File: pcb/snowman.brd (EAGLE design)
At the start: 69.4 x 118.5 mm, 15 parts, among them U1 ATTINY85-20PU

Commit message: update copper trails
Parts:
- added D1, D2, D3, D4: GF1, diode:SMA-DO214AC
- moved R4 9.03 mm to (40.6, 96.5), turned to 110 degrees
- moved R3 4.84 mm to (47.6, 90.8), turned to 170 degrees
- moved R2 4.58 mm to (43.2, 92.7), turned to 140 degrees
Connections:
- new net N$10: D1.K, LS1.N
- new net N$7: D4.K, LS2.N
- new net N$8: D3.K, LS4.N
- new net N$9: D2.K, LS3.N
- net BUZER_HARMONY_1: now also D4.A; no longer LS2.N
- net BUZER_HARMONY_2: now also D3.A; no longer LS4.N
- net BUZER_HARMONY_3: now also D2.A; no longer LS3.N
- net BUZER_MELODY: now also D1.A; no longer LS1.N
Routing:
- net N$7: track 0.00 -> 136.6 mm
- net N$4: track 37.7 -> 171.9 mm
- net N$9: track 0.00 -> 105.5 mm
- net BUZER_HARMONY_3: track 54.3 -> 153.0 mm
- net N$8: track 0.00 -> 85.2 mm
- net BUZER_HARMONY_2: track 88.7 -> 164.3 mm
- net BUZER_HARMONY_1: track 103.6 -> 28.0 mm
- net N$6: track 62.7 -> 95.1 mm
- net N$10: track 0.00 -> 27.2 mm
- net BUZER_MELODY: track 43.5 -> 24.2 mm
- net N$3: track 82.9 -> 77.5 mm
- net N$2: track 65.3 -> 64.8 mm

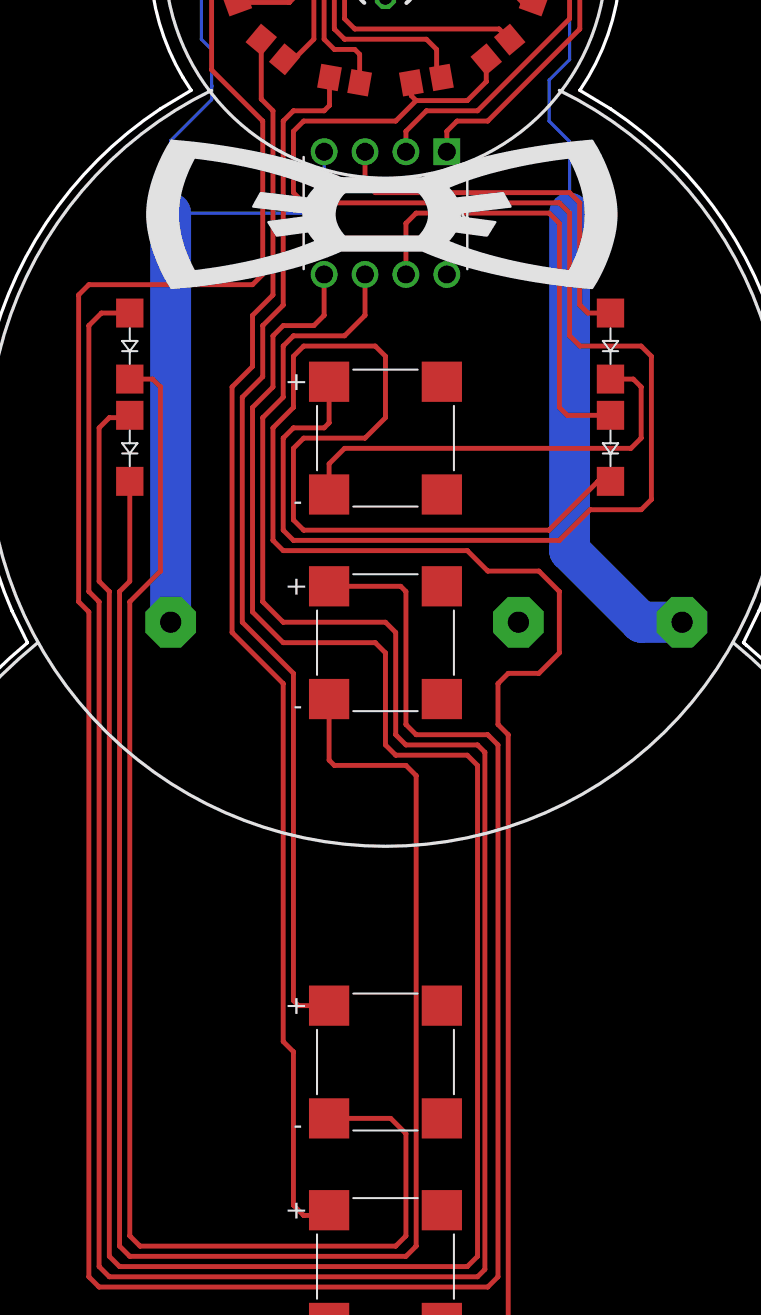
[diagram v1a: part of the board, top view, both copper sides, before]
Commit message: adjust arms
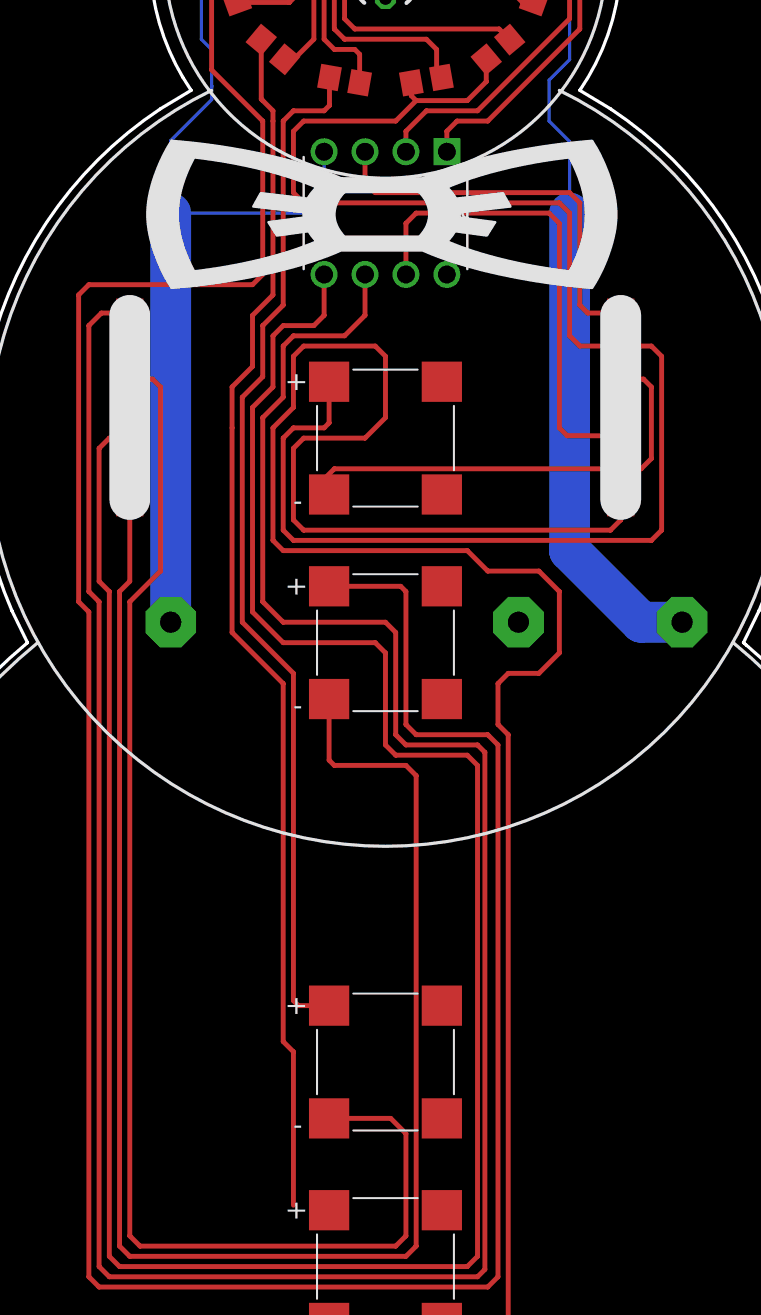
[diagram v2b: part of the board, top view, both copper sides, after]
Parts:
- moved D4 1.42 mm to (64.8, 66.7)
- moved D2 1.27 mm to (34.3, 66.7)
- moved D1 0.63 mm to (64.8, 74.3)
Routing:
- net N$6: track 95.1 -> 97.5 mm
- net N$3: track 77.5 -> 75.3 mm
- net BUZER_HARMONY_1: track 28.0 -> 29.9 mm
- net BUZER_HARMONY_3: track 153.0 -> 151.7 mm
- net N$9: track 105.5 -> 104.2 mm
- net N$7: track 136.6 -> 137.4 mm
- net BUZER_MELODY: track 24.2 -> 24.9 mm

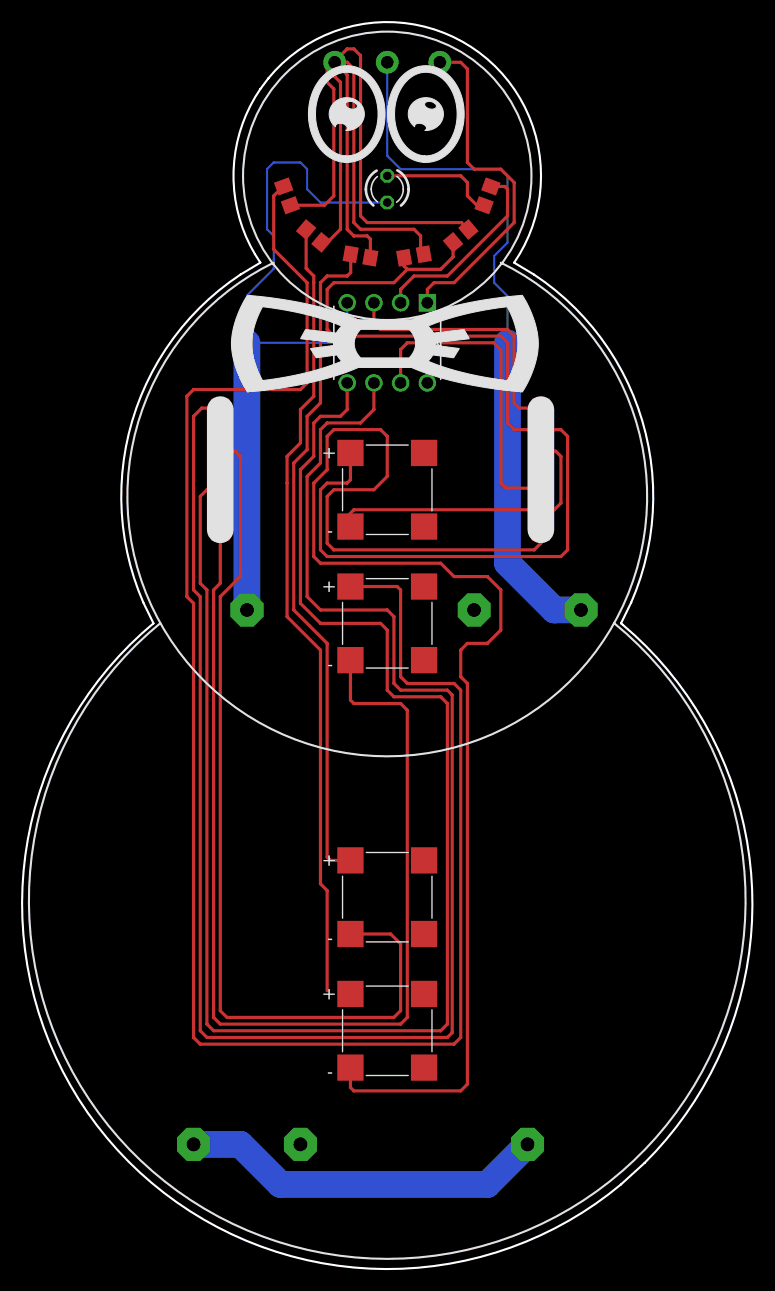
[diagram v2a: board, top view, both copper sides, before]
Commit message: replace component CR-AA -> BLOSSOM-BLM-18650-2PCS
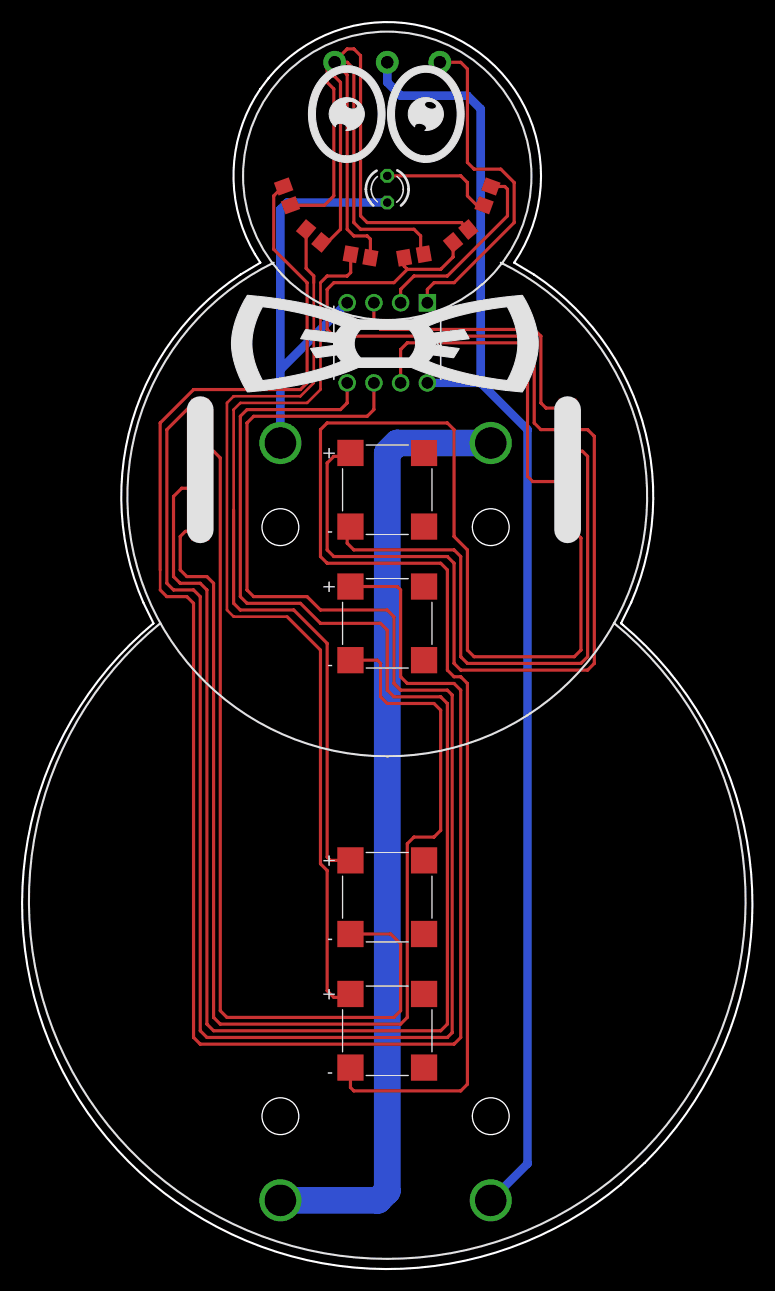
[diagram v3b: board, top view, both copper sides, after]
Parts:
- removed G1, G2: CR-AA, battery:CRAA
- added U$1: BLOSSOM-BLM-18650-2PCS, battery-holders:BLOSSOM-BLM-18650-2PCS
- moved D4 2.62 mm to (67.3, 67.3)
- moved D1 2.54 mm to (67.3, 74.3)
- moved D2 1.91 mm to (32.4, 66.7)
- moved D3 1.91 mm to (32.4, 74.3)
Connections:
- removed net N$1: G1.-, G2.+
- new net N$12: U$1.1, U$1.4
- net GND: now also U$1.2; no longer G2.-
- net VCC: now also U$1.3; no longer G1.+
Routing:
- net N$12: track 0.00 -> 90.9 mm
- net VCC: track 78.9 -> 124.0 mm
- net N$1: track 34.9 -> 0.00 mm
- net GND: track 70.6 -> 41.6 mm
- net N$10: track 27.4 -> 55.9 mm
- net N$6: track 97.5 -> 122.2 mm
- net BUZER_HARMONY_3: track 151.7 -> 166.3 mm
- net BUZER_HARMONY_2: track 164.3 -> 178.5 mm
- net N$3: track 75.3 -> 88.9 mm
- net N$2: track 64.8 -> 76.2 mm
- net N$7: track 137.4 -> 146.6 mm
- net N$9: track 104.2 -> 113.3 mm
- net N$4: track 171.9 -> 175.2 mm
- net BUZER_MELODY: track 24.9 -> 27.4 mm
- net BUZER_HARMONY_1: track 29.9 -> 31.8 mm
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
